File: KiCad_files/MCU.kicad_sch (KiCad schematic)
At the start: 6 parts, among them U1 B3U-1000P, U12 ESP32-S3-MINI-1U

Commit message: puskee
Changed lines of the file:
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@@
+	(wire
+		(pts
+			(xy 144.78 92.71) (xy 151.13 92.71)
+		)
+		(stroke
+			(width 0)
+			(type default)
+		)
+	)
+	(wire
+		(pts
+			(xy 144.78 113.03) (xy 151.13 113.03)
+		)
+		(stroke
+			(width 0)
+			(type default)
+		)
+	)
+	(wire
+		(pts
+			(xy 143.51 48.26) (xy 143.51 50.8)
+		)
+		(stroke
+			(width 0)
+			(type default)
+		)
+	)
+	(wire
+		(pts
+			(xy 144.78 110.49) (xy 151.13 110.49)
+		)
+		(stroke
+			(width 0)
+			(type default)
+		)
+	)
+	(wire
+		(pts
+			(xy 130.81 67.31) (xy 130.81 69.85)
+		)
+		(stroke
+			(width 0)
+			(type default)
+		)
+	)
+	(wire
+		(pts
+			(xy 181.61 110.49) (xy 187.96 110.49)
+		)
+		(stroke
+			(width 0)
+			(type default)
+		)
+	)
+	(wire
+		(pts
+			(xy 130.81 91.44) (xy 130.81 92.71)
+		)
+		(stroke
+			(width 0)
+			(type default)
+		)
+	)
+	(wire
+		(pts
+			(xy 181.61 128.27) (xy 187.96 128.27)
+		)
+		(stroke
+			(width 0)
+			(type default)
+		)
+	)
+	(wire
+		(pts
+			(xy 181.61 115.57) (xy 187.96 115.57)
+		)
+		(stroke
+			(width 0)
+			(type default)
+		)
+	)
+	(wire
+		(pts
+			(xy 181.61 87.63) (xy 187.96 87.63)
+		)
+		(stroke
+			(width 0)
+			(type default)
+		)
+	)
 	(wire
 		(pts
 			(xy 181.61 130.81) (xy 187.96 130.81)
-		)
-		(stroke
-			(width 0)
-			(type default)
-		)
-	)
-	(wire
-		(pts
-			(xy 144.78 92.71) (xy 151.13 92.71)
-		)
-		(stroke
-			(width 0)
-			(type default)
-		)
-	)
-	(wire
-		(pts
-			(xy 144.78 113.03) (xy 151.13 113.03)
-		)
-		(stroke
-			(width 0)
-			(type default)
-		)
-	)
-	(wire
-		(pts
-			(xy 143.51 48.26) (xy 143.51 50.8)
-		)
-		(stroke
-			(width 0)
-			(type default)
-		)
-	)
-	(wire
-		(pts
-			(xy 144.78 110.49) (xy 151.13 110.49)
-		)
-		(stroke
-			(width 0)
-			(type default)
-		)
-	)
-	(wire
-		(pts
-			(xy 130.81 67.31) (xy 130.81 69.85)
-		)
-		(stroke
-			(width 0)
-			(type default)
-		)
-	)
-	(wire
-		(pts
-			(xy 181.61 110.49) (xy 187.96 110.49)
-		)
-		(stroke
-			(width 0)
-			(type default)
-		)
-	)
-	(wire
-		(pts
-			(xy 130.81 91.44) (xy 130.81 92.71)
-		)
-		(stroke
-			(width 0)
-			(type default)
-		)
-	)
-	(wire
-		(pts
-			(xy 181.61 128.27) (xy 187.96 128.27)
-		)
-		(stroke
-			(width 0)
-			(type default)
-		)
-	)
-	(wire
-		(pts
-			(xy 181.61 115.57) (xy 187.96 115.57)
-		)
-		(stroke
-			(width 0)
-			(type default)
-		)
-	)
-	(wire
-		(pts
-			(xy 181.61 87.63) (xy 187.96 87.63)
 		)
 		(stroke
@@
 	(hierarchical_label "BAROMETER_INT"
 		(shape input)
-		(at 205.74 121.92 0)
+		(at 207.01 101.6 0)
+		(effects
+			(font
+				(size 1.27 1.27)
+			)
+			(justify left)
+		)
+	)
+	(hierarchical_label "GNSS_TM"
+		(shape input)
+		(at 207.01 147.32 0)
+		(effects
+			(font
+				(size 1.27 1.27)
+			)
+			(justify left)
+		)
+	)
+	(hierarchical_label "PWM_2"
+		(shape output)
+		(at 207.01 71.12 0)
+		(effects
+			(font
+				(size 1.27 1.27)
+			)
+			(justify left)
+		)
+	)
+	(hierarchical_label "GNSS_HW_S"
+		(shape output)
+		(at 207.01 130.81 0)
 		(effects
 			(font
@@
 	(hierarchical_label "IMU_BOOTN"
 		(shape output)
-		(at 205.74 135.89 0)
+		(at 207.01 115.57 0)
+		(effects
+			(font
+				(size 1.27 1.27)
+			)
+			(justify left)
+		)
+	)
+	(hierarchical_label "GNSS_HW_R"
+		(shape output)
+		(at 207.01 125.73 0)
 		(effects
 			(font
@@
 		)
 	)
+	(hierarchical_label "PWM_3"
+		(shape output)
+		(at 207.01 76.2 0)
+		(effects
+			(font
+				(size 1.27 1.27)
+			)
+			(justify left)
+		)
+	)
 	(hierarchical_label "I2C_SDA"
 		(shape bidirectional)
-		(at 205.74 114.3 0)
+		(at 207.01 93.98 0)
 		(effects
 			(font
@@
 	(hierarchical_label "I2C_CLK"
 		(shape output)
-		(at 205.74 118.11 0)
+		(at 207.01 97.79 0)
 		(effects
 			(font
@@
 	(hierarchical_label "IMU_INT"
 		(shape input)
-		(at 205.74 125.73 0)
+		(at 207.01 105.41 0)
+		(effects
+			(font
+				(size 1.27 1.27)
+			)
+			(justify left)
+		)
+	)
+	(hierarchical_label "PWM_0"
+		(shape output)
+		(at 207.01 63.5 0)
+		(effects
+			(font
+				(size 1.27 1.27)
+			)
+			(justify left)
+		)
+	)
+	(hierarchical_label "UART_RX"
+		(shape input)
+		(at 207.01 142.24 0)
+		(effects
+			(font
+				(size 1.27 1.27)
+			)
+			(justify left)
+		)
+	)
+	(hierarchical_label "UART_TX"
+		(shape output)
+		(at 207.01 135.89 0)
+		(effects
+			(font
+				(size 1.27 1.27)
+			)
+			(justify left)
+		)
+	)
+	(hierarchical_label "GNSS_FIX"
+		(shape input)
+		(at 207.01 120.65 0)
+		(effects
+			(font
+				(size 1.27 1.27)
+			)
+			(justify left)
+		)
+	)
+	(hierarchical_label "PWM_1"
+		(shape output)
+		(at 207.01 67.31 0)
 		(effects
 			(font
@@
 	(hierarchical_label "IMU_NRST"
 		(shape output)
-		(at 205.74 130.81 0)
-		(effects
-			(font
+		(at 207.01 110.49 0)
+		(effects
+			(font

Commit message: johtoja
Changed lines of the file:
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@@
+		)
+	)
+	(hierarchical_label "BAT_STAT"
+		(shape input)
+		(at 207.01 87.63 0)
+		(effects
+			(font
+				(size 1.27 1.27)
+			)
+			(justify left)
 		)
 	)

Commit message: pinnit
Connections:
- net BAROMETER_INT: now also U12.14 (IO10)
- net BAT_STAT: now also U12.7 (IO3)
- net GNSS_FIX: now also U12.8 (IO4)
- net GNSS_HW_R: now also U12.9 (IO5)
- net GNSS_HW_S: now also U12.10 (IO6)
- net GNSS_TM: now also U12.11 (IO7)
- net I2C_CLK: now also U12.13 (IO9)
- net I2C_SDA: now also U12.12 (IO8)
- net IMU_BOOTN: now also U12.17 (IO13)
- net IMU_INT: now also U12.15 (IO11)
- net IMU_NRST: now also U12.16 (IO12)
- net UART_RX: now also U12.22 (IO18)
- net UART_TX: now also U12.21 (IO17)
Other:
- moved on the sheet: U12

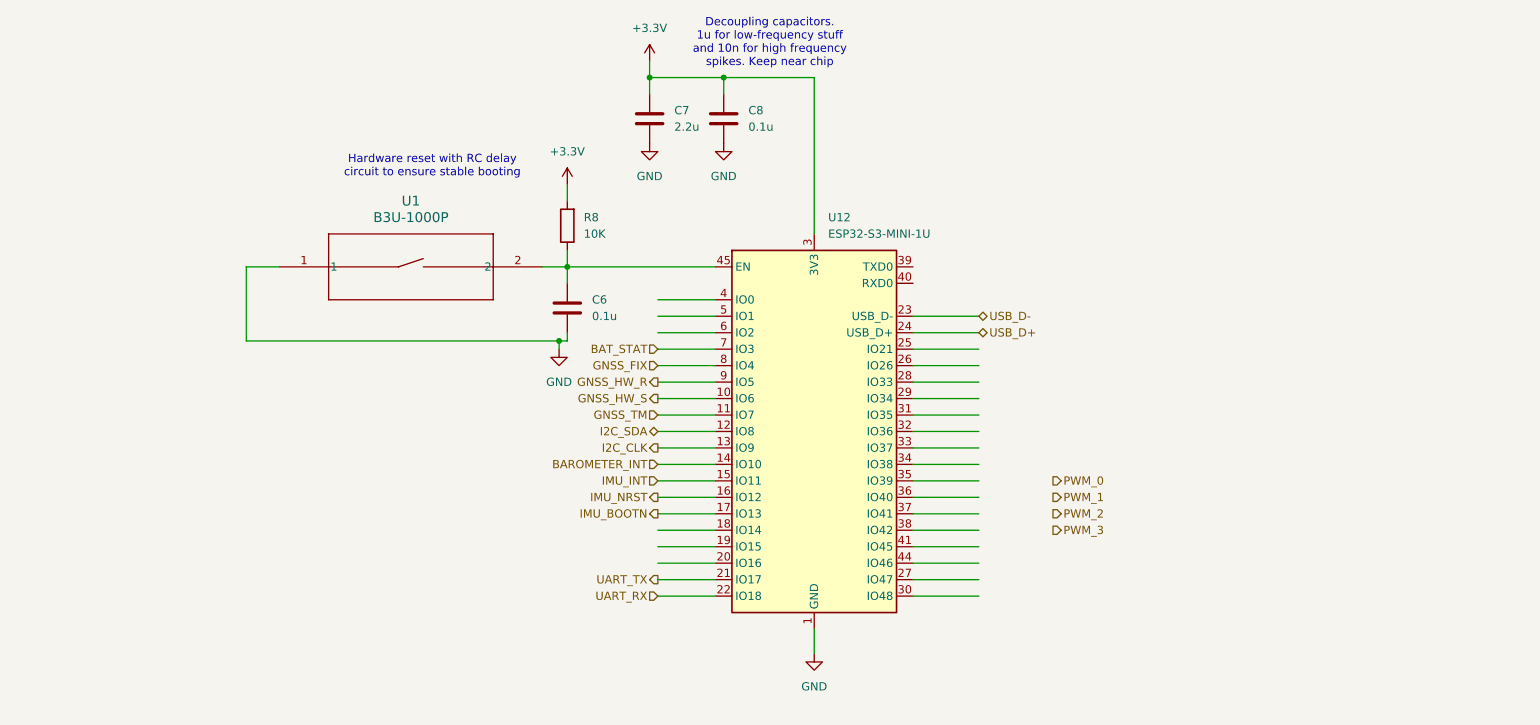
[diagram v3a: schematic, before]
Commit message: piuhat vedetty mculla ja i2c pullupit mculle
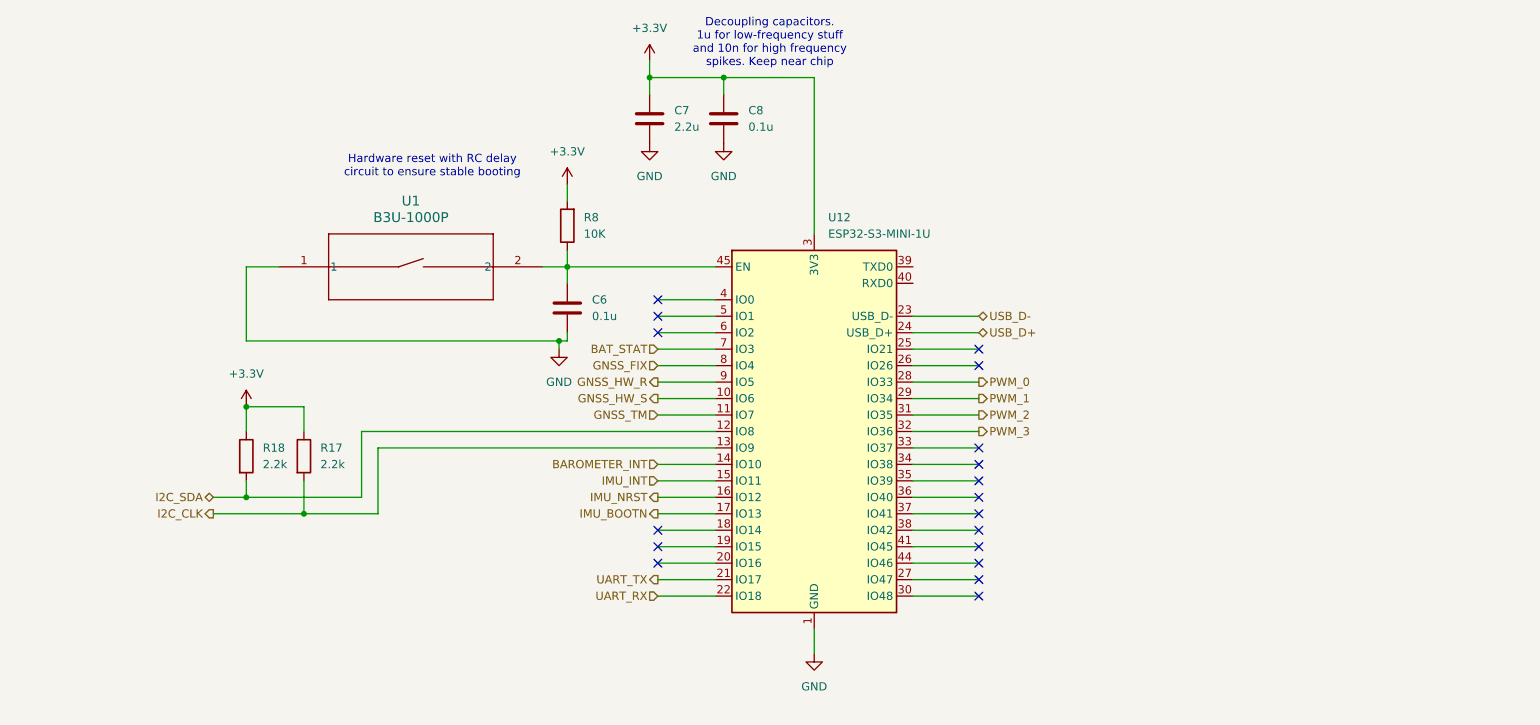
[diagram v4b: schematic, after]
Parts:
- added R17, R18: 2.2k, Resistor_SMD:R_0805_2012Metric_Pad1.20x1.40mm_HandSolder, symbol Device:R
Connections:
- net +3.3V: now also R17.1, R18.1
- net I2C_CLK: now also R17.2
- net I2C_SDA: now also R18.2
- net PWM_0: now also U12.28 (IO33)
- net PWM_1: now also U12.29 (IO34)
- net PWM_2: now also U12.31 (IO35)
- net PWM_3: now also U12.32 (IO36)
- no-connect marks 0 -> 18

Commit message: pinnit
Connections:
- net BAT_STAT: now also U12.32 (IO36); no longer U12.7 (IO3)
- net IMU_BOOTN: now also U12.20 (IO16); no longer U12.17 (IO13)
- net IMU_INT: now also U12.18 (IO14); no longer U12.15 (IO11)
- net IMU_NRST: now also U12.19 (IO15); no longer U12.16 (IO12)
- net PWM_0: now also U12.33 (IO37); no longer U12.28 (IO33)
- net PWM_1: now also U12.34 (IO38); no longer U12.29 (IO34)
- net PWM_2: now also U12.35 (IO39); no longer U12.31 (IO35)
- net PWM_3: now also U12.36 (IO40); no longer U12.32 (IO36)

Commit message: puskee
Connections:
- net GNSS_FIX: now also U12.17 (IO13); no longer U12.8 (IO4)
- net GNSS_HW_R: now also U12.18 (IO14); no longer U12.9 (IO5)
- net GNSS_HW_S: now also U12.19 (IO15); no longer U12.10 (IO6)
- net GNSS_TM: now also U12.20 (IO16); no longer U12.11 (IO7)
- net IMU_BOOTN: now also U12.10 (IO6); no longer U12.20 (IO16)
- net IMU_INT: now also U12.8 (IO4); no longer U12.18 (IO14)
- net IMU_NRST: now also U12.9 (IO5); no longer U12.19 (IO15)

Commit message: JTAG
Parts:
- added R2: 10K, Resistor_SMD:R_0805_2012Metric_Pad1.20x1.40mm_HandSolder, symbol Device:R
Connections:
- net +3.3V: now also R2.2
- net BAT_STAT: now also U12.34 (IO38); no longer U12.32 (IO36)
- net PWM_0: now also U12.35 (IO39); no longer U12.33 (IO37)
- net PWM_1: now also U12.36 (IO40); no longer U12.34 (IO38)
- net PWM_2: now also U12.37 (IO41); no longer U12.35 (IO39)
- net PWM_3: now also U12.38 (IO42); no longer U12.36 (IO40)
- net JTAG_SEL: now reaches U12.7 (IO3)
- net JTAG_SEL: now also R2.1
- no-connect marks 18 -> 17
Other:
- note added: "JTAG inteface GPIO39 GPIO40 GPIO41 GPIO42"
- note added: "Pull JTAG_SEL down during boot to enable auxiliary JTAG interface"
- note added: "Strapping pins: Pins Function Default conf GPIO0 & GPIO46 Chip boot mode GPIO0 PU GPIO45 VDD_SPI voltage PD GPIO46 ROM messages printing PD GPIO3 JTAG signal source select floating"
- note added: "UART0 interface GPIO43 GPIO44"
- moved on the sheet: C6, R8, U1

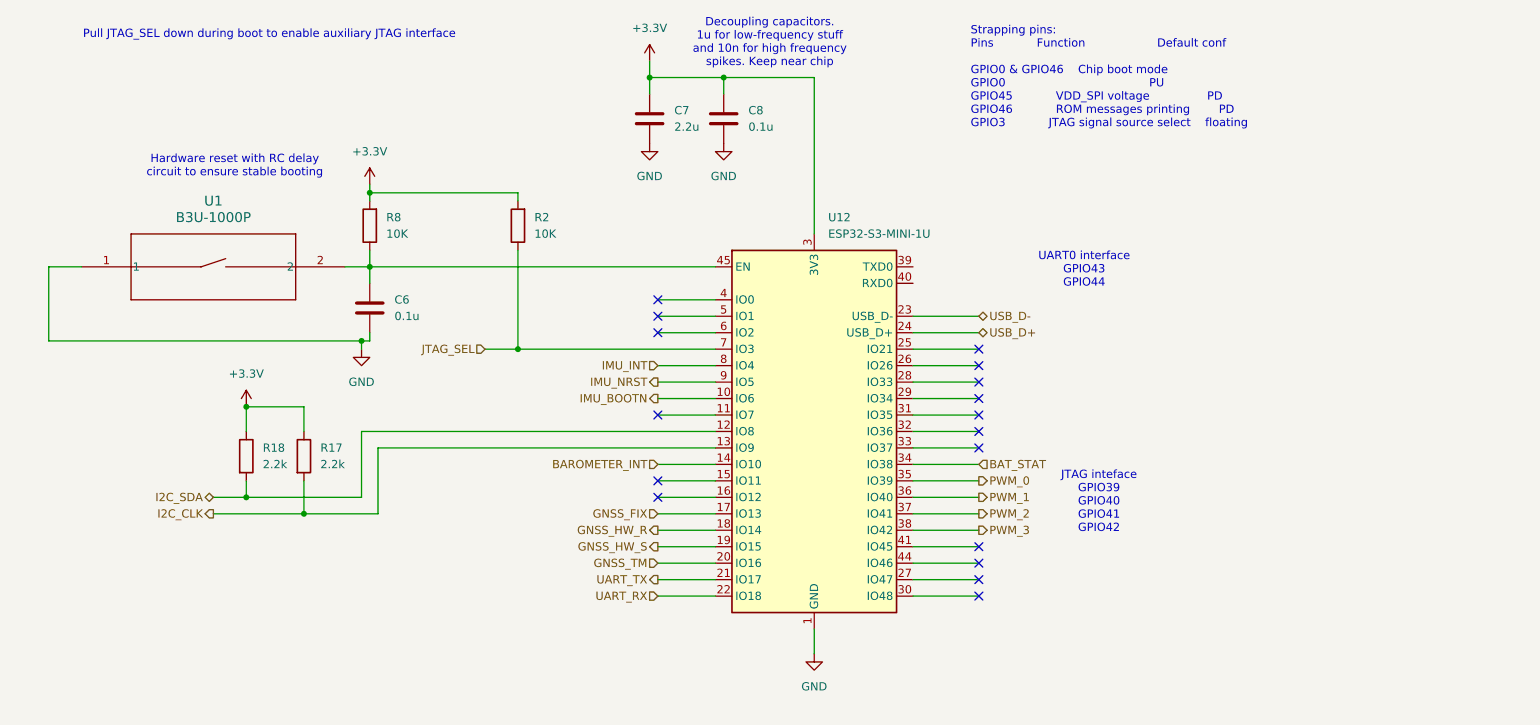
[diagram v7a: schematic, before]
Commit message: ERC hiljennetty
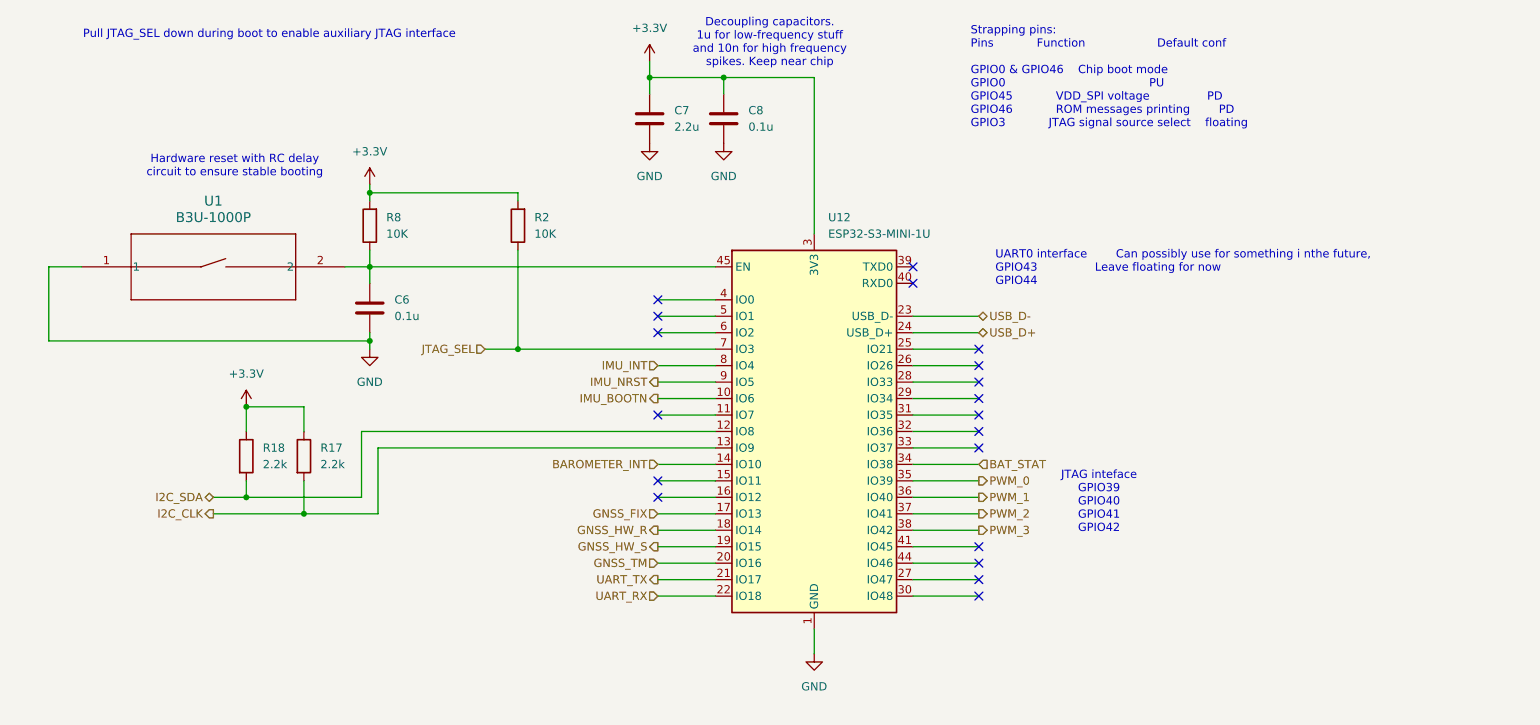
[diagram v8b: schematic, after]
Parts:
- U1: footprint B3U-1000P -> 1_project_library:B3U-1000P
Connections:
- no-connect marks 17 -> 19
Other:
- note added: "UART0 interface Can possibly use for something i nthe future, GPIO43 Leave floating for now GPIO44"
- note removed: "UART0 interface GPIO43 GPIO44"
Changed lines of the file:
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@@
 		)
 	)
-	(text "UART0 interface\nGPIO43\nGPIO44"
+	(text "UART0 interface		Can possibly use for something i nthe future,\nGPIO43				Leave floating for now\nGPIO44"
 		(exclude_from_sim no)
-		(at 210.566 80.518 0)
+		(at 196.85 80.264 0)
 		(effects
 			(font
 				(size 1.27 1.27)
 			)
+			(justify left)
 		)
 	)
@@
 	)
 	(junction
-		(at 99.06 91.44)
-		(diameter 0)
-		(color 0 0 0 0)
-	)
-	(junction
 		(at 100.33 68.58)
 		(diameter 0)
@@
 	)
 	(junction
+		(at 100.33 91.44)
+		(diameter 0)
+		(color 0 0 0 0)
+	)
+	(junction
 		(at 143.51 50.8)
 		(diameter 0)
@@
 	)
 	(no_connect
+		(at 184.15 80.01)
+	)
+	(no_connect
 		(at 144.78 87.63)
+	)
+	(no_connect
+		(at 184.15 82.55)
 	)
 	(no_connect
@@
 	(wire
 		(pts
-			(xy 99.06 91.44) (xy 99.06 92.71)
+			(xy 100.33 91.44) (xy 100.33 92.71)
 		)
 		(stroke
@@
 	(wire
 		(pts
-			(xy 50.8 91.44) (xy 99.06 91.44)
+			(xy 50.8 91.44) (xy 100.33 91.44)
 		)
 		(stroke
@@
 		(pts
 			(xy 81.28 105.41) (xy 81.28 101.6)
-		)
-		(stroke
-			(width 0)
-			(type default)
-		)
-	)
-	(wire
-		(pts
-			(xy 99.06 91.44) (xy 100.33 91.44)
 		)
 		(stroke
@@
 	(symbol
 		(lib_id "power:GND")
-		(at 99.06 92.71 0)
+		(at 100.33 92.71 0)
 		(unit 1)
 		(exclude_from_sim no)
@@
 		(fields_autoplaced yes)
 		(property "Reference" "#PWR026"
-			(at 99.06 99.06 0)
+			(at 100.33 99.06 0)
 			(effects
 				(font
@@
 		)
 		(property "Value" "GND"
-			(at 99.06 97.79 0)
+			(at 100.33 97.79 0)
 			(effects
 				(font
@@
 		)
 		(property "Footprint" ""
-			(at 99.06 92.71 0)
+			(at 100.33 92.71 0)
 			(effects
 				(font
@@
 		)
 		(property "Datasheet" ""
-			(at 99.06 92.71 0)
+			(at 100.33 92.71 0)
 			(effects
 				(font
@@
 		)
 		(property "Description" "Power symbol creates a global label with name \"GND\" , ground"
-			(at 99.06 92.71 0)
+			(at 100.33 92.71 0)
 			(effects
 				(font
@@
 	)
 	(symbol
+		(lib_id "power:+3.3V")
+		(at 143.51 48.26 0)
+		(unit 1)
+		(exclude_from_sim no)
+		(in_bom yes)
+		(on_board yes)
+		(dnp no)
+		(fields_autoplaced yes)
+		(property "Reference" "#PWR05"
+			(at 143.51 52.07 0)
+			(effects
+				(font
+					(size 1.27 1.27)
+				)
+				(hide yes)
+			)
+		)
+		(property "Value" "+3.3V"
+			(at 143.51 43.18 0)
+			(effects
+				(font
+					(size 1.27 1.27)
+				)
+			)
+		)
+		(property "Footprint" ""
+			(at 143.51 48.26 0)
+			(effects
+				(font
+					(size 1.27 1.27)
+				)
+				(hide yes)
+			)
+		)
+		(property "Datasheet" ""
+			(at 143.51 48.26 0)
+			(effects
+				(font
+					(size 1.27 1.27)
+				)
+				(hide yes)
+			)
+		)
+		(property "Description" "Power symbol creates a global label with name \"+3.3V\""
+			(at 143.51 48.26 0)
+			(effects
+				(font
+					(size 1.27 1.27)
+				)
+				(hide yes)
+			)
+		)
+		(pin "1"
+		)
+		(instances
+			(project "esp"
+				(path "/186d5500-054c-4b47-a89c-85f6ce2abe33/da295ba5-5e07-44a9-8c1c-e3f6c5500b46"
+					(reference "#PWR05")
+					(unit 1)
+				)
+			)
+		)
+	)
+	(symbol
 		(lib_id "1_projektin osat:B3U-1000P")
 		(at 55.88 80.01 0)
@@
 			)
 		)
-		(property "Footprint" "B3U-1000P"
+		(property "Footprint" "1_project_library:B3U-1000P"
 			(at 55.88 80.01 0)
 			(effects
@@
 		)
 		(property "DigiKey" "SW1020CT-ND"
-			(at 55.88 80.01 0)
-			(effects
-				(font
-					(size 1.27 1.27)
-				)
-				(hide yes)
-			)
-		)
-		(property "MNF PART NUMBER" ""
 			(at 55.88 80.01 0)
 			(effects
@@
 					(unit 1)
 				)
-			)
-		)
-	)
-	(symbol
-		(lib_id "power:+3.3V")
-		(at 143.51 48.26 0)
-		(unit 1)
-		(exclude_from_sim no)
-		(in_bom yes)
-		(on_board yes)
-		(dnp no)
-		(fields_autoplaced yes)
-		(property "Reference" "#PWR027"
-			(at 143.51 52.07 0)
-			(effects
-				(font
-					(size 1.27 1.27)
-				)
-				(hide yes)
-			)
-		)
-		(property "Value" "+3.3V"
-			(at 143.51 43.18 0)
-			(effects
-				(font
-					(size 1.27 1.27)
-				)
-			)
-		)
-		(property "Footprint" ""
-			(at 143.51 48.26 0)
-			(effects
-				(font
-					(size 1.27 1.27)
-				)
-				(hide yes)
-			)
-		)
-		(property "Datasheet" ""
-			(at 143.51 48.26 0)
-			(effects
-				(font
-					(size 1.27 1.27)
-				)
-				(hide yes)
-			)
-		)
-		(property "Description" "Power symbol creates a global label with name \"+3.3V\""
-			(at 143.51 48.26 0)
-			(effects
-				(font
-					(size 1.27 1.27)
-				)
-				(hide yes)
-			)
-		)
-		(pin "1"
-		)
-		(instances
-			(project "esp"
-				(path "/186d5500-054c-4b47-a89c-85f6ce2abe33/da295ba5-5e07-44a9-8c1c-e3f6c5500b46"
-					(reference "#PWR027")
-					(unit 1)
-				)
